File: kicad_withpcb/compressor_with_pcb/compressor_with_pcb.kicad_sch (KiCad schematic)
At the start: 167 parts, among them J1 EDA 306, J2 FRONT BOARD, Q1 BC549C, Q2 BC549C, Q3 BC549C, Q4 BC549C, Q5 BC549C, Q6 BC549C, Q7 BC549C, Q8 BC549C, Q9 BC549C, SW1 BYPASS, SW2 INT/EXT, SW3 HPF DEFEAT, SW4 LINK, U1 NE5532, U10 LM3915, U2 NE5532, U3 NE5532, U4 TL072, U5 NE5532, U6 NE5532, U7 NE5532, U9 LM3914

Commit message: Split Q2's collector from the VCA tail and update the README (#3)
* Split Q2's collector from the VCA tail

A wire at x = 62.23 mm joined Q2's collector (with Q8 and Q9) to the
tail node (Q3, R14, R15). They are now two nets: Net-(Q2-C) on Q2.1,
Q8.3 and Q9.3, and Net-(Q3-C) on Q3.1, R14.1 and R15.2. The board has
the new pad nets but not yet the copper to match.

* Re-route the tail net around R14, R15 and Q3

Two B.Cu stubs still carried Net-(Q2-C) onto the tail pads: one from the
Q8/Q9 link down to R14.1, and one from the via at (138.4, 69.8) to
R15.2. Both are gone. The existing R15.2 to Q3.1 track is now on
Net-(Q3-C), and R14.1 runs on F.Cu up between +16V and BYP_A, along
y = 73.3 to a new via at (143, 72.85), then on B.Cu to R15.2. Zones
refilled.

DRC: 0 errors, 0 unconnected, schematic parity clean (the two existing
warnings remain).

* Bring the README up to date with the routed boards
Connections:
- net at Q3.1 (C), R14.1, R15.2: no longer Q2.1 (C), Q8.3 (E), Q9.3 (E)
- new net: Q2.1 (C), Q8.3 (E), Q9.3 (E)
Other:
- note added: "Front board connector Pots, switches and both meters (U9, U10, D20-D36)"
- note removed: "Front board connector Pots, switches and both meters (U9, U10, D20-D36) are on the front board: see ../compressor_front. They stay drawn here, excluded from this board and its BOM."
- moved on the sheet: C15, D7, J2, Q2, R15, R45, R46, R47, RV4, RV5, RV6, SW4

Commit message: Simulate the compressor, fix its values, and fit Altronics parts (#5)
* Make the schematic simulate in KiCad, and add the simulation results

Every part on the kicad/ sheets now has a SPICE model (Sim.* fields, models in
kicad/sim/compressor_models.lib), the connectors are excluded from simulation, and the
root sheet carries a test bench: the rack's supplies, a balanced source, a load and the
knob settings as .param lines. The netlist is unchanged.

tools/add_sim_models.py writes the fields. tools/sim/run_all.py exports the netlist with
kicad-cli and runs the characterisation in ngspice; kicad/sim/README.md has how to run
it in KiCad and what it found.

* Bring the compressor's values in line with the design targets

Through gain: R21/R22 3k3 to 6k8 halves the recovery amp's gain, so the
module is unity balanced in to out and BYPASS matches; R36 100k to 200k
keeps the detector's level. Bass: C9/C10 2u2 to 4u7 with the larger
input resistors puts the -3 dB point near 5 Hz.
Threshold: RV3 1M linear to 250k audio taper and R35 20k to 2k4 spread
about -20 to +20 dBu over the knob. R60 47k to 24k sets the resting
steer near 150 mV.
Timing: R45/R46/RV5 and R47/RV6/R74 scaled up to match the RC targets
with the same C15.

Same changes on the sheets, both boards and design.py. The simulation's
pot model gains an audio taper, and the burst test now runs at half
threshold.

* Carry the new values onto both boards' schematics and layouts

* Retune attack and release: R45 220R, R46 47R, RV5 10k, R47 15k

The first pass ran the attack too slow (9 to 103 ms against a 2.7 to
50 ms target). Results are regenerated in the next commit.

* Regenerate the simulation results for the new values

* Stop the fast-attack overshoot: C22 47u to 4u7

C22 made STA lag STB by about 60 ms, so when CTRL-B pulled the
reference node down the steering kept moving after the control
voltage had settled, overshooting by up to 20 dB. With 4u7 the two
sides track and the overshoot is about 1 dB. RV5 back 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
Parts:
- C10, C9: value 2u2 -> 4u7; footprint Capacitor_THT:C_Rect_L7.0mm_W2.5mm_P5.00mm -> Capacitor_THT:C_Rect_L16.5mm_W7.3mm_P15.00mm_MKT
- C14: value 220n -> 2u2; footprint Capacitor_THT:C_Rect_L7.0mm_W2.5mm_P5.00mm -> Capacitor_THT:C_Rect_L7.2mm_W7.2mm_P5.00mm_FKS2_FKP2_MKS2_MKP2
- C15, C5, C8: footprint Capacitor_THT:C_Rect_L7.0mm_W2.5mm_P5.00mm -> Capacitor_THT:C_Rect_L16.5mm_W11.8mm_P15.00mm_MKT
- C22: value 47u -> 4u7
- C35: footprint Capacitor_THT:C_Rect_L7.0mm_W2.5mm_P5.00mm -> Capacitor_THT:C_Rect_L7.2mm_W7.2mm_P5.00mm_FKS2_FKP2_MKS2_MKP2
- R21, R22: value 3k3 -> 6k8
- R35: value 20k -> 1k
- R36: value 100k -> 82k
- R38: value 10k -> 1k
- R47: value 4k7 -> 15k
- R60: value 47k -> 24k
- RV3: value 1M -> 100kA
- RV5: value 4k7 -> 10k
- RV6: value 220k -> 1M
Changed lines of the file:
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@@
 			)
 		)
-		(property "Value" "220k"
+		(property "Value" "1M"
 			(at 140.97 180.34 90)
 			(show_name no)
@@
 			)
 		)
-		(property "Footprint" "Capacitor_THT:C_Rect_L7.0mm_W2.5mm_P5.00mm"
+		(property "Footprint" "Capacitor_THT:C_Rect_L16.5mm_W11.8mm_P15.00mm_MKT"
 			(at 50.8 62.23 0)
 			(hide yes)
@@
 			)
 		)
-		(property "Value" "20k"
+		(property "Value" "1k"
 			(at 85.09 128.016 90)
 			(show_name no)
@@
 			)
 		)
-		(property "Value" "2u2"
+		(property "Value" "4u7"
 			(at 96.52 50.8 90)
 			(show_name no)
@@
 			)
 		)
-		(property "Footprint" "Capacitor_THT:C_Rect_L7.0mm_W2.5mm_P5.00mm"
+		(property "Footprint" "Capacitor_THT:C_Rect_L16.5mm_W7.3mm_P15.00mm_MKT"
 			(at 91.44 52.07 0)
 			(hide yes)
@@
 			)
 		)
-		(property "Value" "4k7"
+		(property "Value" "15k"
 			(at 154.178 180.34 90)
 			(show_name no)
@@
 			)
 		)
-		(property "Value" "3k3"
+		(property "Value" "6k8"
 			(at 97.79 73.914 90)
 			(show_name no)
@@
 			)
 		)
-		(property "Value" "47u"
+		(property "Value" "4u7"
 			(at 58.674 222.758 90)
 			(show_name no)
@@
 			)
 		)
-		(property "Footprint" "Capacitor_THT:C_Rect_L7.0mm_W2.5mm_P5.00mm"
+		(property "Footprint" "Capacitor_THT:C_Rect_L16.5mm_W11.8mm_P15.00mm_MKT"
 			(at 44.45 48.26 0)
 			(hide yes)
@@
 			)
 		)
-		(property "Value" "100k"
+		(property "Value" "82k"
 			(at 108.204 130.81 90)
 			(show_name no)
@@
 			)
 		)
-		(property "Value" "2u2"
+		(property "Value" "4u7"
 			(at 98.044 85.344 90)
 			(show_name no)
@@
 			)
 		)
-		(property "Footprint" "Capacitor_THT:C_Rect_L7.0mm_W2.5mm_P5.00mm"
+		(property "Footprint" "Capacitor_THT:C_Rect_L16.5mm_W7.3mm_P15.00mm_MKT"
 			(at 96.52 80.01 0)
 			(hide yes)
@@
 			)
 		)
-		(property "Value" "3k3"
+		(property "Value" "6k8"
 			(at 100.838 54.356 90)
 			(show_name no)
@@
 			)
 		)
-		(property "Value" "10k"
+		(property "Value" "1k"
 			(at 64.516 136.398 90)
 			(show_name no)
@@
 			)
 		)
-		(property "Footprint" "Capacitor_THT:C_Rect_L7.0mm_W2.5mm_P5.00mm"
+		(property "Footprint" "Capacitor_THT:C_Rect_L7.2mm_W7.2mm_P5.00mm_FKS2_FKP2_MKS2_MKP2"
 			(at 340.36 138.43 0)
 			(hide yes)
@@
 			)
 		)
-		(property "Footprint" "Capacitor_THT:C_Rect_L7.0mm_W2.5mm_P5.00mm"
+		(property "Footprint" "Capacitor_THT:C_Rect_L16.5mm_W11.8mm_P15.00mm_MKT"
 			(at 128.27 186.69 0)
 			(hide yes)
@@
 			)
 		)
-		(property "Value" "4k7"
+		(property "Value" "10k"
 			(at 98.552 180.34 90)
 			(show_name no)
@@
 			)
 		)
-		(property "Value" "1M"
+		(property "Value" "100kA"
 			(at 72.136 122.682 90)
 			(show_name no)
@@
 			)
 		)
-		(property "Value" "47k"
+		(property "Value" "24k"
 			(at 30.48 220.218 90)
 			(show_name no)
@@
 			)
 		)
-		(property "Value" "220n"
+		(property "Value" "2u2"
 			(at 53.34 129.54 90)
 			(show_name no)
@@
 			)
 		)
-		(property "Footprint" "Capacitor_THT:C_Rect_L7.0mm_W2.5mm_P5.00mm"
+		(property "Footprint" "Capacitor_THT:C_Rect_L7.2mm_W7.2mm_P5.00mm_FKS2_FKP2_MKS2_MKP2"
 			(at 57.15 128.27 0)
 			(hide yes)

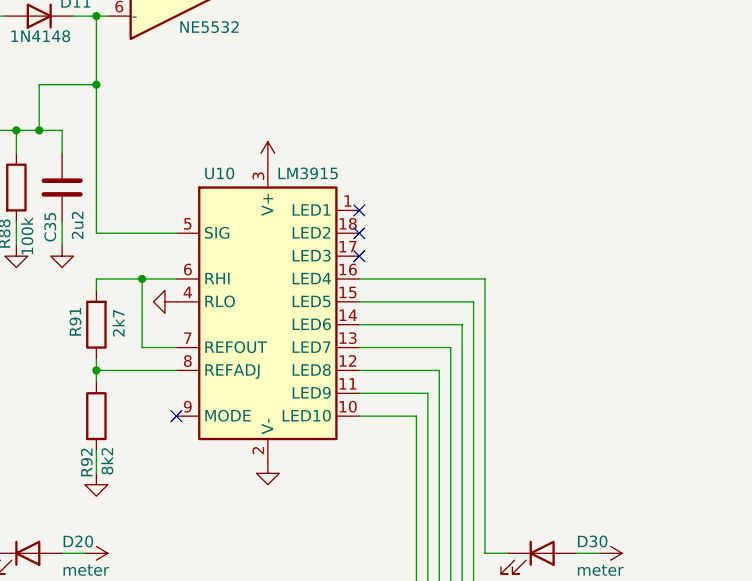
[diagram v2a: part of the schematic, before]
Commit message: Swap the level meter's LM3915 for an LM3914 on outputs 1-7
Nobody stocks the LM3915, so U10 becomes a second LM3914. The LEDs move
to outputs 1-7 and outputs 8-10 join the top LED, giving a 17 dB scale
with no added parts. Front board LVL tracks re-routed; BOM regenerated.
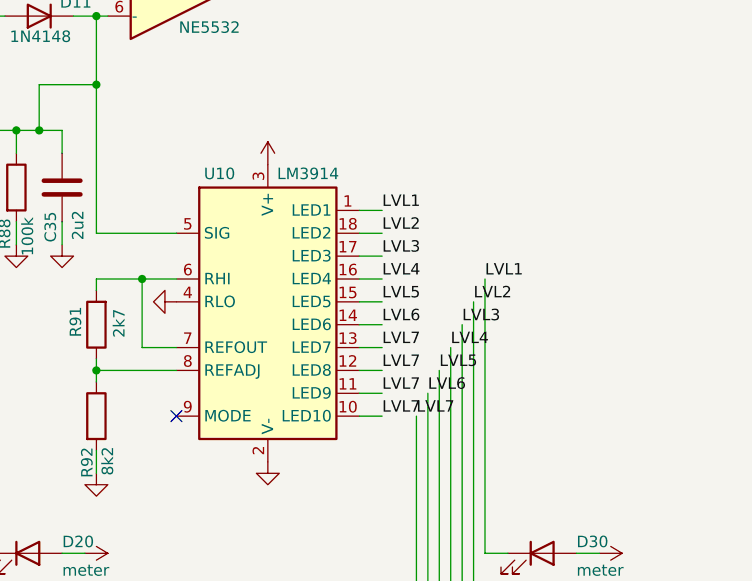
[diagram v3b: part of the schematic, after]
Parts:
- U10: value LM3915 -> LM3914
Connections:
- net LVL1: now reaches D30.1 (K)
- net LVL1: now also U10.1 (LED1); no longer U10.16 (LED4)
- net LVL3: now reaches D32.1 (K)
- net LVL3: now also U10.17 (LED3); no longer U10.14 (LED6)
- net LVL6: now reaches D35.1 (K)
- net LVL6: now also U10.14 (LED6); no longer U10.11 (LED9)
- net LVL7: now reaches D36.1 (K), U10.10 (LED10)
- net LVL7: now also U10.11 (LED9), U10.12 (LED8), U10.13 (LED7)
- net LVL5: now reaches D34.1 (K)
- net LVL5: now also U10.15 (LED5); no longer U10.12 (LED8)
- net LVL4: now reaches D33.1 (K)
- net LVL4: now also U10.16 (LED4); no longer U10.13 (LED7)
- net LVL2: now reaches D31.1 (K)
- net LVL2: now also U10.18 (LED2); no longer U10.15 (LED5)
- no-connect marks 8 -> 5
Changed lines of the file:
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@@
 	)
 	(no_connect
-		(at 373.38 143.51)
-	)
-	(no_connect
-		(at 373.38 140.97)
-	)
-	(no_connect
 		(at 295.91 163.83)
 	)
 	(no_connect
-		(at 373.38 146.05)
-	)
-	(no_connect
 		(at 316.23 158.75)
 	)
@@
 	(wire
 		(pts
-			(xy 373.38 156.21) (xy 383.54 156.21)
-		)
-		(stroke
-			(width 0)
-			(type default)
-		)
-	)
-	(wire
-		(pts
 			(xy 389.89 217.17) (xy 379.73 217.17)
 		)
@@
 	(wire
 		(pts
-			(xy 373.38 148.59) (xy 387.35 148.59)
-		)
-		(stroke
-			(width 0)
-			(type default)
-		)
-	)
-	(wire
-		(pts
 			(xy 337.82 127) (xy 344.17 127)
 		)
@@
 	(wire
 		(pts
-			(xy 373.38 153.67) (xy 384.81 153.67)
-		)
-		(stroke
-			(width 0)
-			(type default)
-		)
-	)
-	(wire
-		(pts
 			(xy 63.5 93.98) (xy 69.85 93.98)
 		)
@@
 	(wire
 		(pts
-			(xy 373.38 151.13) (xy 386.08 151.13)
-		)
-		(stroke
-			(width 0)
-			(type default)
-		)
-	)
-	(wire
-		(pts
 			(xy 144.78 219.71) (xy 144.78 217.17)
 		)
@@
 	(wire
 		(pts
-			(xy 379.73 163.83) (xy 373.38 163.83)
-		)
-		(stroke
-			(width 0)
-			(type default)
-		)
-	)
-	(wire
-		(pts
 			(xy 43.18 88.9) (xy 63.5 88.9)
 		)
@@
 	(wire
 		(pts
-			(xy 373.38 161.29) (xy 381 161.29)
-		)
-		(stroke
-			(width 0)
-			(type default)
-		)
-	)
-	(wire
-		(pts
 			(xy 209.55 139.7) (xy 213.36 139.7)
 		)
@@
 	(wire
 		(pts
-			(xy 373.38 158.75) (xy 382.27 158.75)
-		)
-		(stroke
-			(width 0)
-			(type default)
-		)
-	)
-	(wire
-		(pts
 			(xy 109.22 227.33) (xy 109.22 229.87)
 		)
@@
 			)
 		)
-		(property "Value" "LM3915"
+		(property "Value" "LM3914"
 			(at 364.236 136.906 0)
 			(show_name no)
@@
 		)
 	)
+	(label "LVL1"
+		(at 387.35 148.59 0)
+		(fields_autoplaced yes)
+		(effects
+			(font
+				(size 1.27 1.27)
+			)
+			(justify left bottom)
+		)
+	)
+	(label "LVL2"
+		(at 386.08 151.13 0)
+		(fields_autoplaced yes)
+		(effects
+			(font
+				(size 1.27 1.27)
+			)
+			(justify left bottom)
+		)
+	)
+	(label "LVL3"
+		(at 384.81 153.67 0)
+		(fields_autoplaced yes)
+		(effects
+			(font
+				(size 1.27 1.27)
+			)
+			(justify left bottom)
+		)
+	)
+	(label "LVL4"
+		(at 383.54 156.21 0)
+		(fields_autoplaced yes)
+		(effects
+			(font
+				(size 1.27 1.27)
+			)
+			(justify left bottom)
+		)
+	)
+	(label "LVL5"
+		(at 382.27 158.75 0)
+		(fields_autoplaced yes)
+		(effects
+			(font
+				(size 1.27 1.27)
+			)
+			(justify left bottom)
+		)
+	)
+	(label "LVL6"
+		(at 381 161.29 0)
+		(fields_autoplaced yes)
+		(effects
+			(font
+				(size 1.27 1.27)
+			)
+			(justify left bottom)
+		)
+	)
+	(label "LVL7"
+		(at 379.73 163.83 0)
+		(fields_autoplaced yes)
+		(effects
+			(font
+				(size 1.27 1.27)
+			)
+			(justify left bottom)
+		)
+	)
+	(wire
+		(pts
+			(xy 373.38 163.83) (xy 375.92 163.83)
+		)
+		(stroke
+			(width 0)
+			(type default)
+		)
+	)
+	(label "LVL7"
+		(at 375.92 163.83 0)
+		(fields_autoplaced yes)
+		(effects
+			(font
+				(size 1.27 1.27)
+			)
+			(justify left bottom)
+		)
+	)
+	(wire
+		(pts
+			(xy 373.38 161.29) (xy 375.92 161.29)
+		)
+		(stroke
+			(width 0)
+			(type default)
+		)
+	)
+	(label "LVL7"
+		(at 375.92 161.29 0)
+		(fields_autoplaced yes)
+		(effects
+			(font
+				(size 1.27 1.27)
+			)
+			(justify left bottom)
+		)
+	)
+	(wire
+		(pts
+			(xy 373.38 158.75) (xy 375.92 158.75)
+		)
+		(stroke
+			(width 0)
+			(type default)
+		)
+	)
+	(label "LVL7"
+		(at 375.92 158.75 0)
+		(fields_autoplaced yes)
+		(effects
+			(font
+				(size 1.27 1.27)
+			)
+			(justify left bottom)
+		)
+	)
+	(wire
+		(pts
+			(xy 373.38 156.21) (xy 375.92 156.21)
+		)
+		(stroke
+			(width 0)
+			(type default)
+		)
+	)
+	(label "LVL7"
+		(at 375.92 156.21 0)
+		(fields_autoplaced yes)
+		(effects
+			(font
+				(size 1.27 1.27)
+			)
+			(justify left bottom)
+		)
+	)
+	(wire
+		(pts
+			(xy 373.38 153.67) (xy 375.92 153.67)
+		)
+		(stroke
+			(width 0)
+			(type default)
+		)
+	)
+	(label "LVL6"
+		(at 375.92 153.67 0)
+		(fields_autoplaced yes)
+		(effects
+			(font
+				(size 1.27 1.27)
+			)
+			(justify left bottom)
+		)
+	)
+	(wire
+		(pts
+			(xy 373.38 151.13) (xy 375.92 151.13)
+		)
+		(stroke
+			(width 0)
+			(type default)
+		)
+	)
+	(label "LVL5"
+		(at 375.92 151.13 0)
+		(fields_autoplaced yes)
+		(effects
+			(font
+				(size 1.27 1.27)
+			)
+			(justify left bottom)
+		)
+	)
+	(wire
+		(pts
+			(xy 373.38 148.59) (xy 375.92 148.59)
+		)
+		(stroke
+			(width 0)
+			(type default)
+		)
+	)
+	(label "LVL4"
+		(at 375.92 148.59 0)
+		(fields_autoplaced yes)
+		(effects
+			(font
+				(size 1.27 1.27)
+			)
+			(justify left bottom)
+		)
+	)
+	(wire
+		(pts
+			(xy 373.38 146.05) (xy 375.92 146.05)
+		)
+		(stroke
+			(width 0)
+			(type default)
+		)
+	)
+	(label "LVL3"
+		(at 375.92 146.05 0)
+		(fields_autoplaced yes)
+		(effects
+			(font
+				(size 1.27 1.27)
+			)
+			(justify left bottom)
+		)
+	)
+	(wire
+		(pts
+			(xy 373.38 143.51) (xy 375.92 143.51)
+		)
+		(stroke
+			(width 0)
+			(type default)
+		)
+	)
+	(label "LVL2"
+		(at 375.92 143.51 0)
+		(fields_autoplaced yes)
+		(effects
+			(font
+				(size 1.27 1.27)
+			)
+			(justify left bottom)
+		)
+	)
+	(wire
+		(pts
+			(xy 373.38 140.97) (xy 375.92 140.97)
+		)
+		(stroke
+			(width 0)
+			(type default)
+		)
+	)
+	(label "LVL1"
+		(at 375.92 140.97 0)
+		(fields_autoplaced yes)
+		(effects
+			(font
+				(size 1.27 1.27)
+			)
+			(justify left bottom)
+		)
+	)

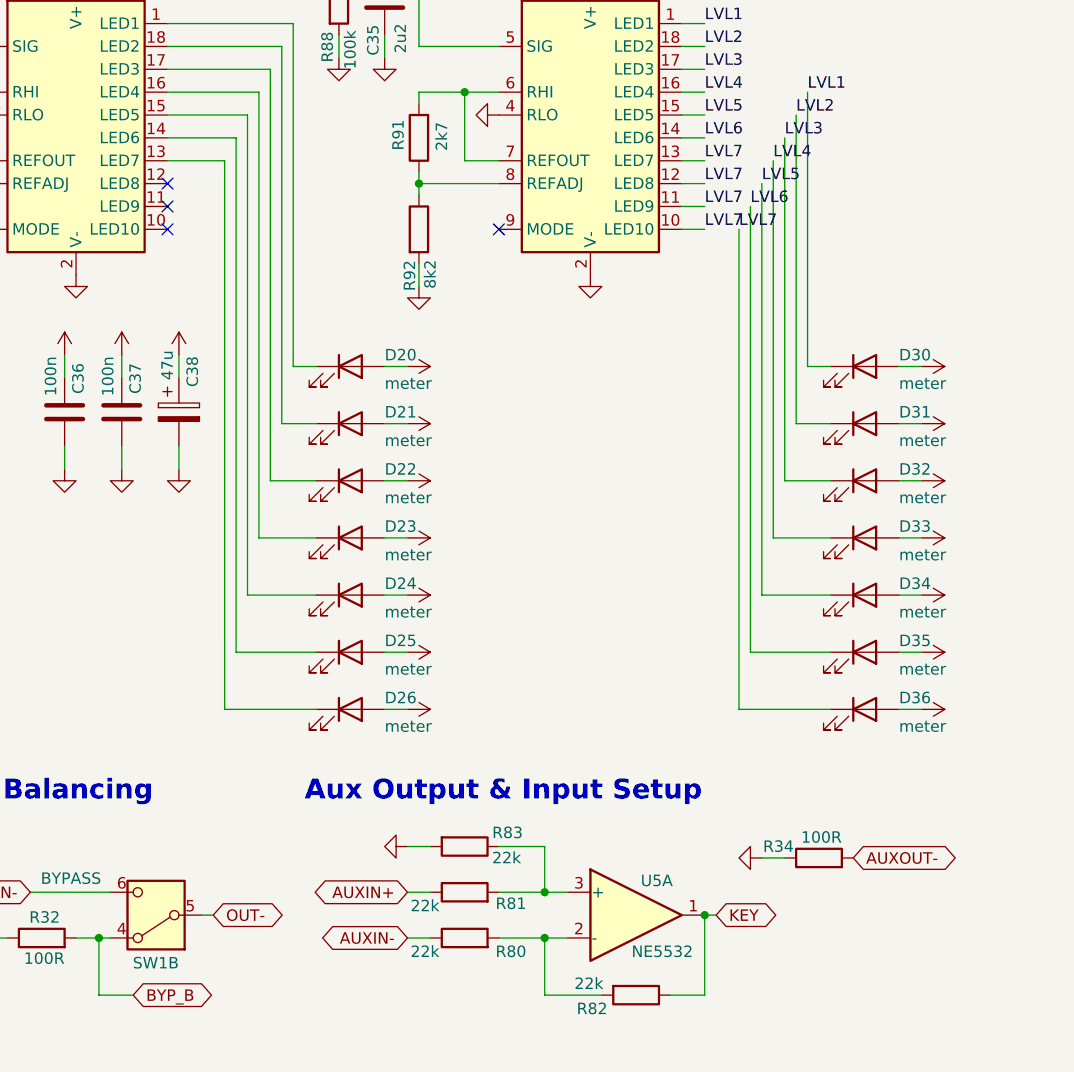
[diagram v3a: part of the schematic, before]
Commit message: Give both meters ten LEDs and simulate them
Adds D27-D29 (GR outputs 8-10) and D37-D39 (LVL outputs 8-10) on all three
schematics. The front board's meter columns move to a 3.0 mm pitch with
LVL output 10 at the top; R90/R92 move to a 7.62 mm footprint and C38
turns to clear the LEDs; the affected nets were re-routed. R92 becomes 4k7
so RV8 can set the top LED at +18 dBu. The panel gets the six extra holes.
The LM3914 sim model now has its comparators and LED current sinks, and
tools/sim/meters.py simulates both meters.
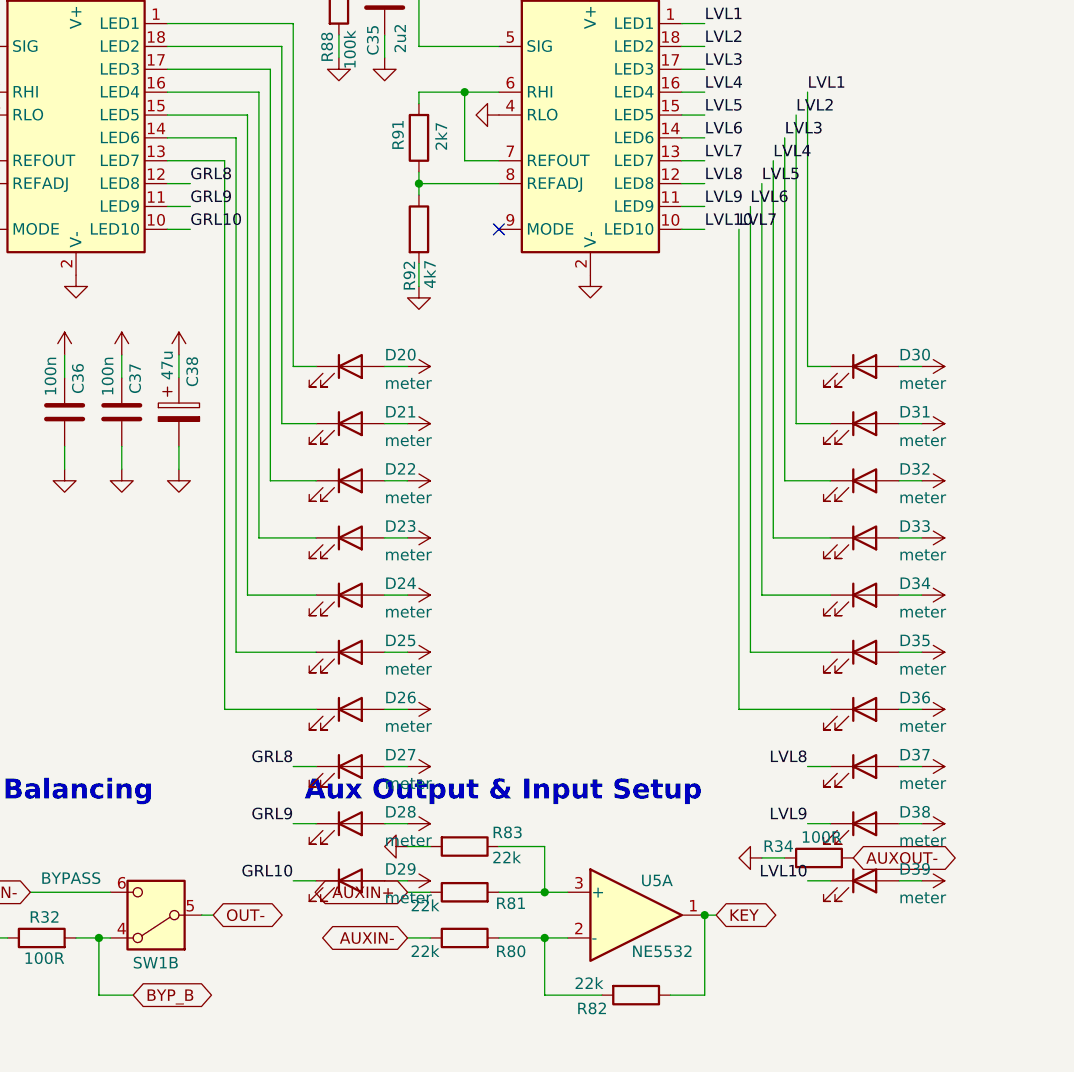
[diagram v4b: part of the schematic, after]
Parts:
- added D27, D28, D29, D37, D38, D39: meter, LED_THT:LED_D2.0mm_W4.0mm_H2.8mm_FlatTop, symbol Device:LED
- R90: footprint Resistor_THT:R_Axial_DIN0207_L6.3mm_D2.5mm_P10.16mm_Horizontal -> Resistor_THT:R_Axial_DIN0207_L6.3mm_D2.5mm_P7.62mm_Horizontal
- R92: value 8k2 -> 4k7; footprint Resistor_THT:R_Axial_DIN0207_L6.3mm_D2.5mm_P10.16mm_Horizontal -> Resistor_THT:R_Axial_DIN0207_L6.3mm_D2.5mm_P7.62mm_Horizontal
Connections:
- net +16V: now also D27.2 (A), D28.2 (A), D29.2 (A), D37.2 (A), D38.2 (A), D39.2 (A)
- net LVL7: no longer U10.10 (LED10), U10.11 (LED9), U10.12 (LED8)
- net GRL10: now reaches U9.10 (LED10)
- net GRL10: now also D29.1 (K)
- net GRL9: now reaches U9.11 (LED9)
- net GRL9: now also D28.1 (K)
- net GRL8: now reaches U9.12 (LED8)
- net GRL8: now also D27.1 (K)
- new net LVL10: D39.1 (K), U10.10 (LED10)
- new net LVL8: D37.1 (K), U10.12 (LED8)
- new net LVL9: D38.1 (K), U10.11 (LED9)
- no-connect marks 5 -> 2
